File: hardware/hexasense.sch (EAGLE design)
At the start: 15 parts, among them IC1 AT45DB161D-SU

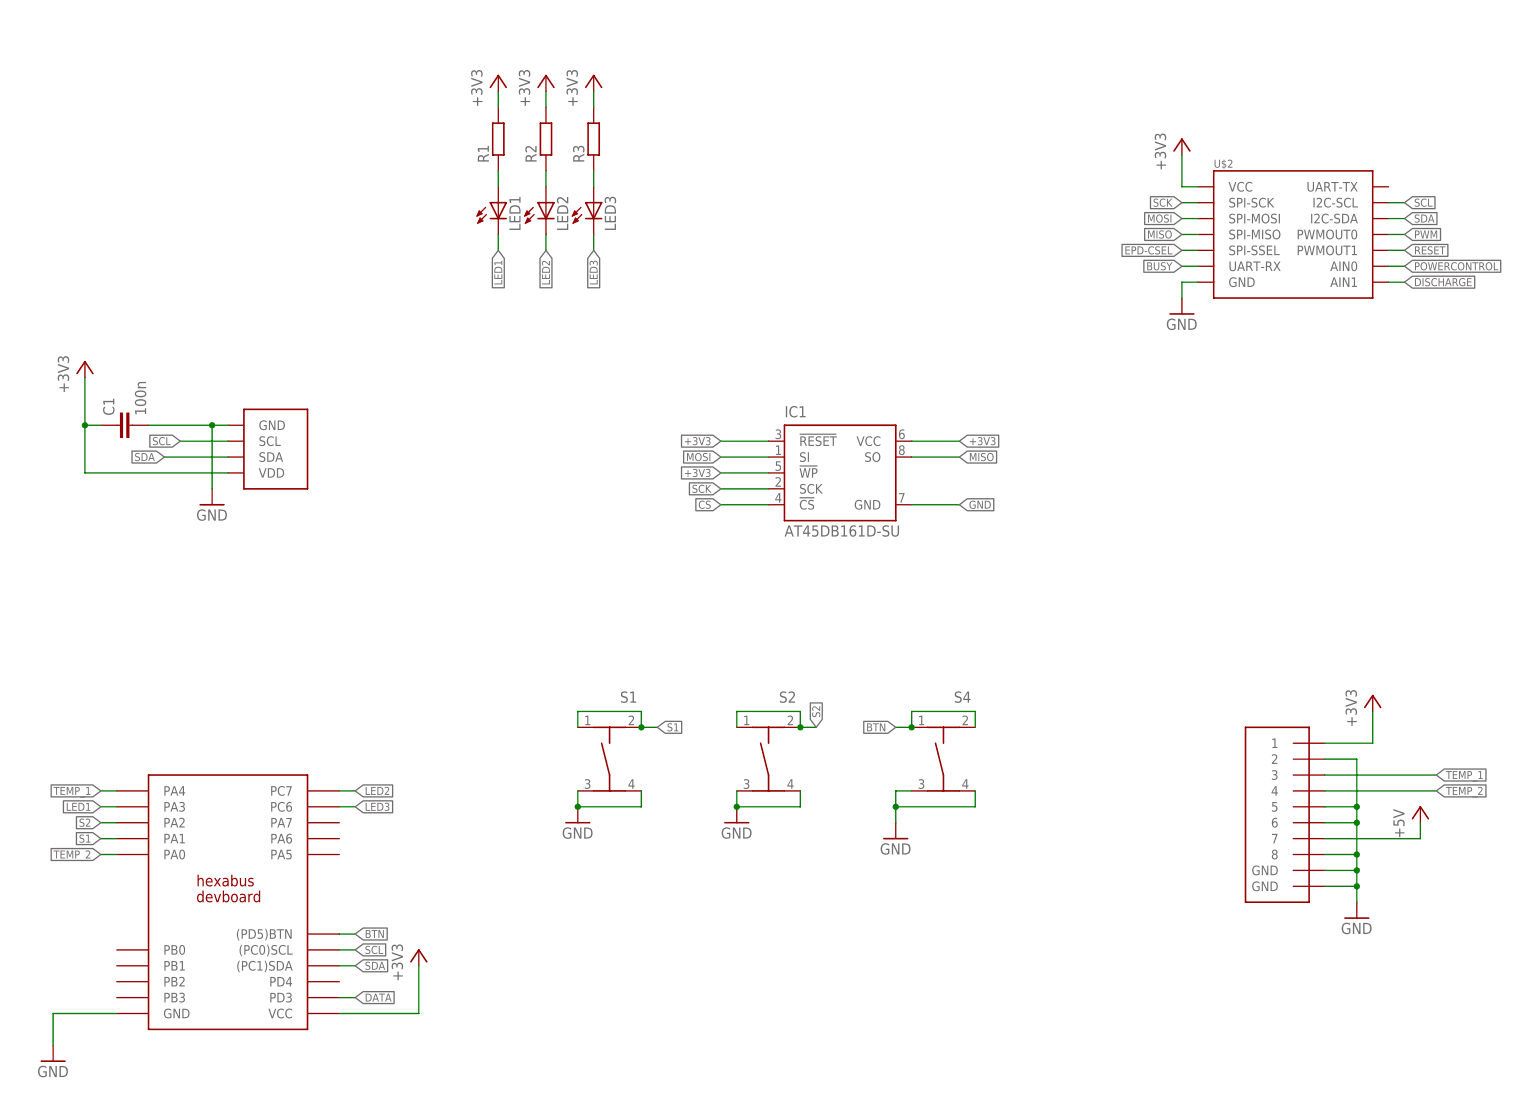
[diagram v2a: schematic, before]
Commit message: added missing wires
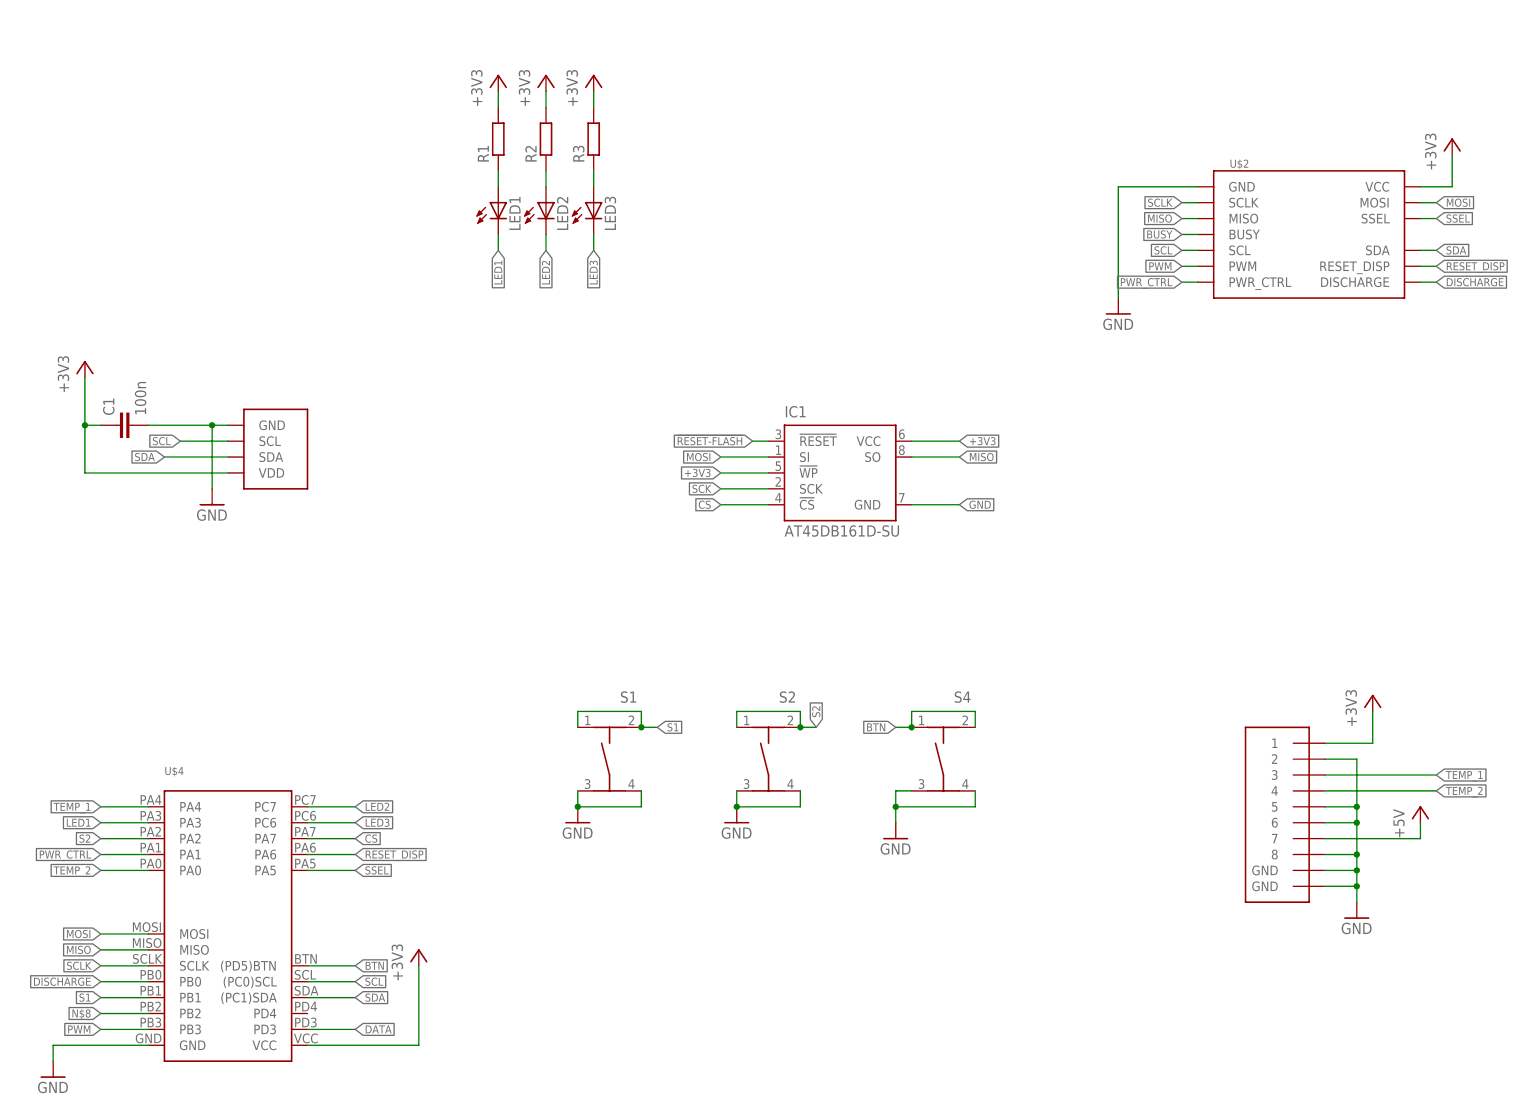
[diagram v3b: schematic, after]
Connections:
- removed net EPD-CSEL: U$2.SPI-SSEL
- removed net POWERCONTROL: U$2.AIN0
- removed net RESET: U$2.PWMOUT1
- new net !RESET-FLASH: IC1.!RESET
- new net N$8: U$4.PB2
- new net PWR_CTRL: U$2.PWR_CTRL, U$4.PA1
- new net RESET_DISP: U$2.RESET_DISP, U$4.PA6
- new net SCLK: U$2.SCLK, U$4.SCLK
- new net SSEL: U$2.SSEL, U$4.PA5
- net +3V3: no longer IC1.!RESET
- net BUSY: now also U$2.BUSY; no longer U$2.UART-RX
- net CS: now also U$4.PA7
- net DISCHARGE: now also U$2.DISCHARGE, U$4.PB0; no longer U$2.AIN1
- net MISO: now also U$2.MISO, U$4.MISO; no longer U$2.SPI-MISO
- net MOSI: now also U$2.MOSI, U$4.MOSI; no longer U$2.SPI-MOSI
- net PWM: now also U$2.PWM, U$4.PB3; no longer U$2.PWMOUT0
- net S1: now also U$4.PB1; no longer U$4.PA1
- net SCK: no longer U$2.SPI-SCK
- net SCL: now also U$2.SCL; no longer U$2.I2C-SCL
- net SDA: now also U$2.SDA; no longer U$2.I2C-SDA

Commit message: added reset and SCLK line for flash chip
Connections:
- removed net SCK: IC1.SCK
- net !RESET-FLASH: now also U$4.PD4
- net SCLK: now also IC1.SCK
